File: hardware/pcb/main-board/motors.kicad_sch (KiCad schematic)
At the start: 0 parts

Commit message: Start of driver schematic
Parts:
- added C12: 0.47 uF, symbol Device:C
- added J12, J13: Conn_01x11_Socket, Connector_JST:JST_PH_B11B-PH-K_1x11_P2.00mm_Vertical, symbol Connector:Conn_01x11_Socket
- added R26: 10k, Resistor_SMD:R_1206_3216Metric_Pad1.30x1.75mm_HandSolder, symbol Device:R_US
- added U6, U7: DRV8436PWPR, PWP0028P_TSSOP_TEX, symbol DRV8436PWPR:DRV8436PWPR
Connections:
- new net: R26.1, U6.16 (NFAULT)
- new net +24V: U6.13 (VM), U6.2 (VM), U7.13 (VM), U7.2 (VM)
- new net DVDD: C12.1, R26.2, U6.15 (DVDD), U6.19 (TOFF)
- new net GND: C12.2, U6.12 (PGND), U6.14 (GND), U6.18 (M0), U6.21 (DECAY0), U6.22 (M1), U6.3 (PGND), U7.12 (PGND), U7.14 (GND), U7.3 (PGND)
- new net Stepper 1 Coil 1 +: J12.3 (Pin_3), U6.5 (AOUT1)
- new net Stepper 1 Coil 1 -: J12.5 (Pin_5), U6.6 (AOUT2)
- new net Stepper 1 Coil 2 +: J12.7 (Pin_7), U6.9 (BOUT2)
- new net Stepper 1 Coil 2 -: J12.9 (Pin_9), U6.10 (BOUT1)
- new net Stepper 2 Coil 1 +: J13.3 (Pin_3), U7.5 (AOUT1)
- new net Stepper 2 Coil 1 -: J13.5 (Pin_5), U7.6 (AOUT2)
- new net Stepper 2 Coil 2 +: J13.7 (Pin_7), U7.9 (BOUT2)
- new net Stepper 2 Coil 2 -: J13.9 (Pin_9), U7.10 (BOUT1)
- no-connect marks 0 -> 14

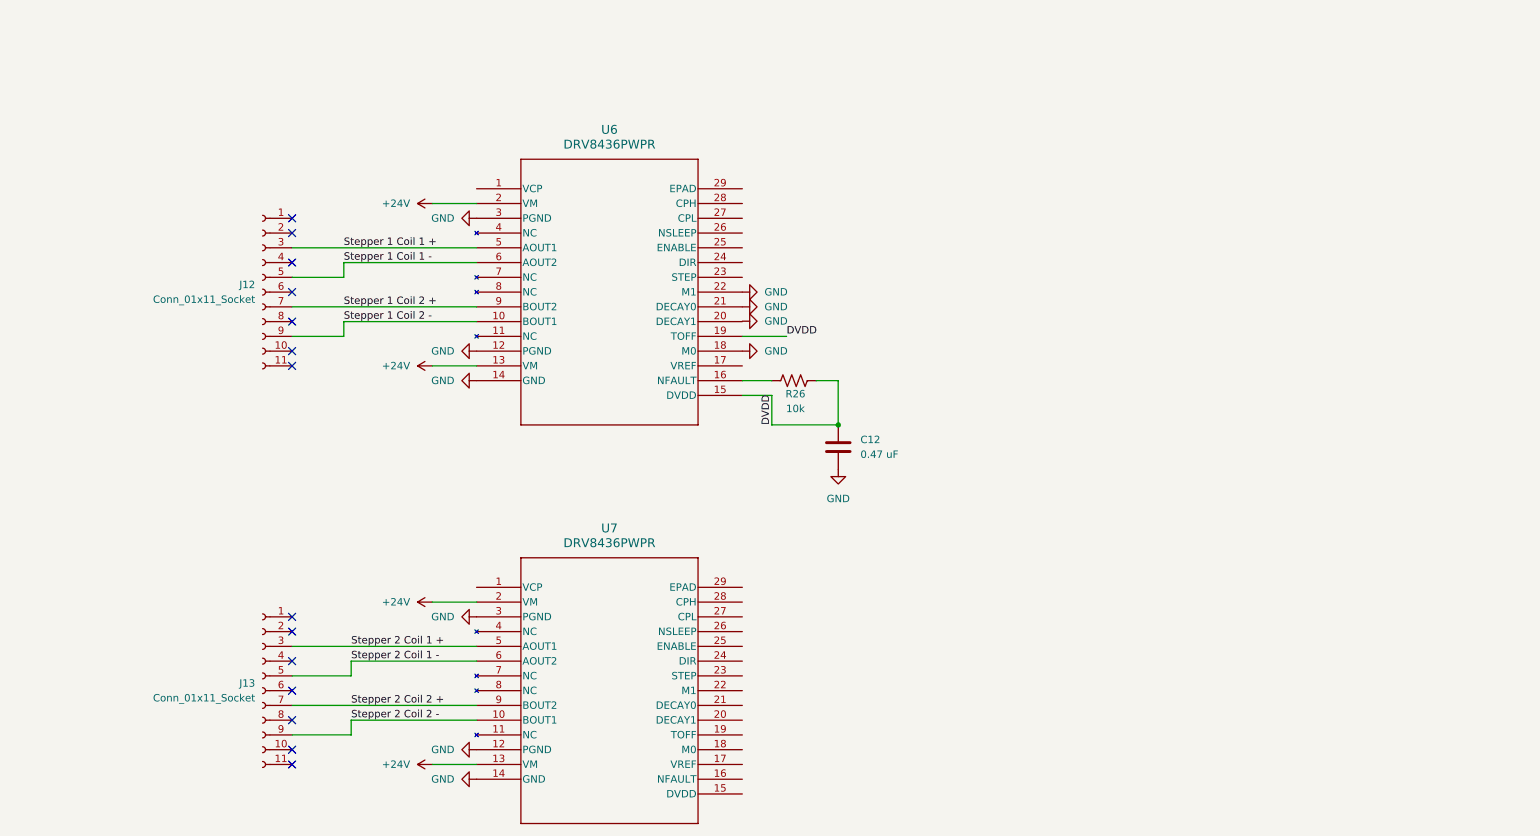
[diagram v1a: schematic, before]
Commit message: Stepper drivers (real)
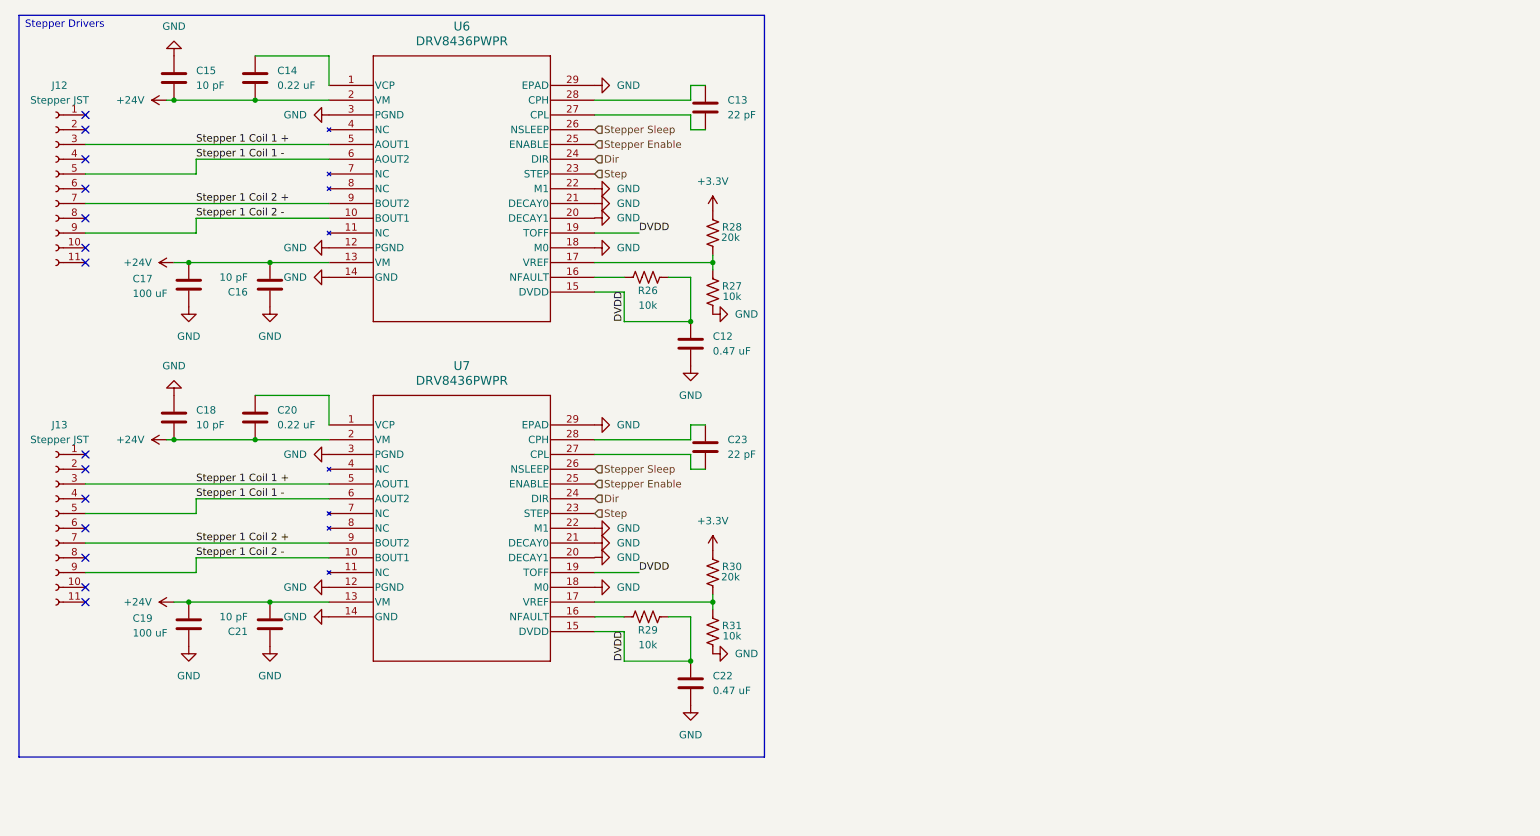
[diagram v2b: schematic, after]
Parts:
- added C13, C23: 22 pF, symbol Device:C
- added C14, C20: 0.22 uF, symbol Device:C
- added C15, C16, C18, C21: 10 pF, symbol Device:C
- added C17, C19: 100 uF, symbol Device:C
- added C22: 0.47 uF, symbol Device:C
- added R27, R29, R31: 10k, Resistor_SMD:R_1206_3216Metric_Pad1.30x1.75mm_HandSolder, symbol Device:R_US
- added R28, R30: 20k, Resistor_SMD:R_1206_3216Metric_Pad1.30x1.75mm_HandSolder, symbol Device:R_US
- J12, J13: value Conn_01x11_Socket -> Stepper JST
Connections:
- net Stepper 2 Coil 1 + is gone; now on net Stepper 1 Coil 1 +: J13.3 (Pin_3), U7.5 (AOUT1)
- net Stepper 2 Coil 1 - is gone; now on net Stepper 1 Coil 1 -: J13.5 (Pin_5), U7.6 (AOUT2)
- net Stepper 2 Coil 2 + is gone; now on net Stepper 1 Coil 2 +: J13.7 (Pin_7), U7.9 (BOUT2)
- net Stepper 2 Coil 2 - is gone; now on net Stepper 1 Coil 2 -: J13.9 (Pin_9), U7.10 (BOUT1)
- net +24V: now also C14.2, C15.2, C16.2, C17.2, C18.2, C19.2, C20.2, C21.2
- net DVDD: now also U7.15 (DVDD), U7.19 (TOFF), C22.1, R29.2
- net GND: now also U6.29 (EPAD), U7.18 (M0), U7.21 (DECAY0), U7.22 (M1), U7.29 (EPAD), C15.1, C16.1, C17.1, C18.1, C19.1, C21.1, C22.2, R27.1, R31.1
- net at U7.1 (VCP): now also C20.1
- net at U7.16 (NFAULT): now also R29.1
- net at U7.17 (VREF): now also R30.1, R31.2
- net Step: now reaches U7.23 (STEP)
- net Step: now also U6.23 (STEP)
- net Dir: now reaches U7.24 (DIR)
- net Dir: now also U6.24 (DIR)
- net Stepper Enable: now reaches U7.25 (ENABLE)
- net Stepper Enable: now also U6.25 (ENABLE)
- net Stepper Sleep: now reaches U7.26 (NSLEEP)
- net Stepper Sleep: now also U6.26 (NSLEEP)
- net at U7.27 (CPL): now also C23.2
- net at U7.28 (CPH): now also C23.1
- net at U6.1 (VCP): now also C14.1
- net at U6.17 (VREF): now also R27.2, R28.1
- net at U6.27 (CPL): now also C13.2
- net at U6.28 (CPH): now also C13.1
- new net +3.3V: R28.2, R30.2
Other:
- note added: "Stepper Drivers"
- moved on the sheet: C12, J12, R26, U6

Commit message: Start of CAN-FD
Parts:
- added D10, D13: MMBZ27VCLT1G, MMBZ27VCLT1G:SOT-23-3_1P4X3P040_ONS, symbol Power_Protection:RCLAMP0502B
- added J14: CAN-FD Port, Package_DFN_QFN:Nordic_AQFN-94-1EP_7x7mm_P0.4mm, symbol Connector:Conn_01x02_Pin
- added U8: MCP2517FDT-H/SL, SOP_MCP2517FDT-H/SL_MCH, symbol MCP2517FDT-H/SL:MCP2517FDT-H_SL
- added U9: ATA6563-GAQW1, SOIC8_SN_MCH, symbol ATA6563_GAQW1:ATA6563-GAQW1
- U6: footprint PWP0028P_TSSOP_TEX -> DRV8436PWPR:PWP0028P_TSSOP_TEX
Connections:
- net GND: now also D10.1 (K1), D13.2 (K2)
- new net: D13.1 (K1), J14.2 (Pin_2)
- new net: D10.2 (K2), J14.1 (Pin_1)
- no-connect marks 14 -> 16

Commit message: Start of CAN-FD
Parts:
- added C24, C25: 0.47 uF, symbol Device:C
- added C26: 4.7 nF, symbol Device:C
- added R32, R33: 60.4, Resistor_SMD:R_1206_3216Metric_Pad1.30x1.75mm_HandSolder, symbol Device:R_US
- added Y1: 40 MHz, Oscillator:Oscillator_SMD_SiTime_PQFD-6L_3.2x2.5mm, symbol Device:Crystal
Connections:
- net +3.3V: now also U9.5 (VIO)
- net GND: now also U8.7 (VSS), U9.2 (GND), C24.2, C25.1, C26.1
- net CANL: now reaches D13.1 (K1), J14.2 (Pin_2)
- net CANL: now also U9.6 (CANL), C25.2, R33.1
- net CANH: now reaches D10.2 (K2), J14.1 (Pin_1)
- net CANH: now also U9.7 (CANH), C24.1, R32.2
- net TX_CAN: now reaches U8.1 (TXCAN)
- net TX_CAN: now also U9.1 (TXD)
- net SCK: now reaches U8.10 (SCK)
- net MOSI: now reaches U8.11 (SDI)
- net MISO: now reaches U8.12 (SDO)
- net CS: now reaches U8.13 (nCS)
- net RX_CAN: now reaches U8.2 (RXCAN)
- net RX_CAN: now also U9.4 (RXD)
- net CLK0: now reaches U8.3 (CLKO/SOF)
- net OSC2: now reaches U8.5 (OSC2)
- net OSC2: now also Y1.2
- net OSC1: now reaches U8.6 (OSC1)
- net OSC1: now also Y1.1
- net xSTBY: now reaches U8.9 (INT0/GPIO0/XSTBY)
- net xSTBY: now also U9.8 (STBY)
- net +5V: now reaches U9.3 (VCC)
- new net: C26.2, R32.1, R33.2
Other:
- note added: "CAN-FD Port"
- note added: "Note: Configuring MCP2517 pin 9 to xSTBY allows it to put the transiever in standby mode directly. That will be useful in future, but may cause debuging problems?"
- moved on the sheet: D10, D13, J14, U8, U9

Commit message: CAN-FD Transceiver Done
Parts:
- removed U8: MCP2517FDT-H/SL, SOP_MCP2517FDT-H/SL_MCH, symbol MCP2517FDT-H/SL:MCP2517FDT-H_SL
- removed Y1: 40 MHz, Oscillator:Oscillator_SMD_SiTime_PQFD-6L_3.2x2.5mm, symbol Device:Crystal
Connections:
- net xSTBY renamed CAN Standby
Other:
- note added: "CAN-FD Transceiver"
- note removed: "Note: Configuring MCP2517 pin 9 to xSTBY allows it to put the transiever in standby mode directly. That will be useful in future, but may cause debuging problems?"
- moved on the sheet: C24, C25, C26, D10, D13, J14, R32, R33, U9

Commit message: RS485 Comms
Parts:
- added C27, C28: 0.1 uF, symbol Device:C
- added C29: 10 uF, symbol Device:C
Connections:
- net +3.3V: now also C27.2
- net +5V: now also C28.2, C29.2
- net GND: now also C27.1, C28.1, C29.1
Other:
- moved on the sheet: U9
